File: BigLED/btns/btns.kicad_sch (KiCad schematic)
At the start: 25 parts, among them J1 MainBrd, J2 Prog, J3 DBG, SW1 TSX101G100-250, SW2 RotaryEncoder_Switch, SW3 SW_Push, SW4 SW_Push, SW5 SW_Push, SW6 SW_Push, SW7 SW_Push, SW8 SW_Push, SW9 SW_Push, U1 PY32F002AF15P6TU, U3 74LVC2G66, U4 SSD1306 OLED

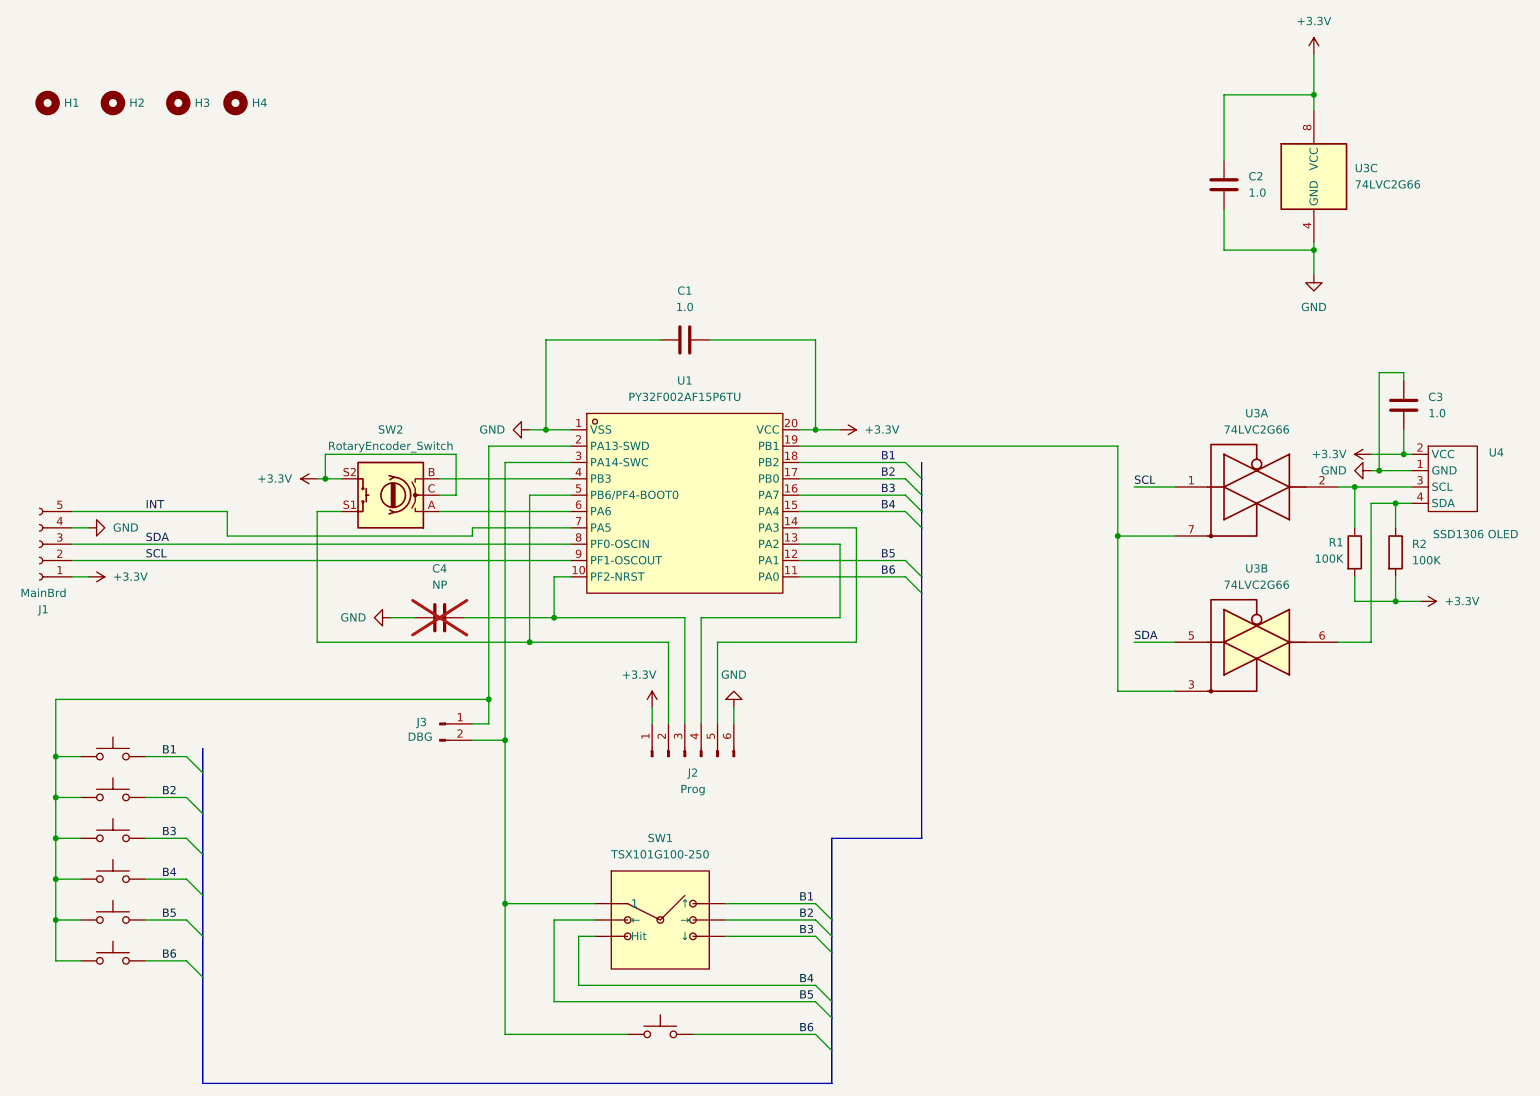
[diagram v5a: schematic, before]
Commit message: PCB for BigLED Buttons finished
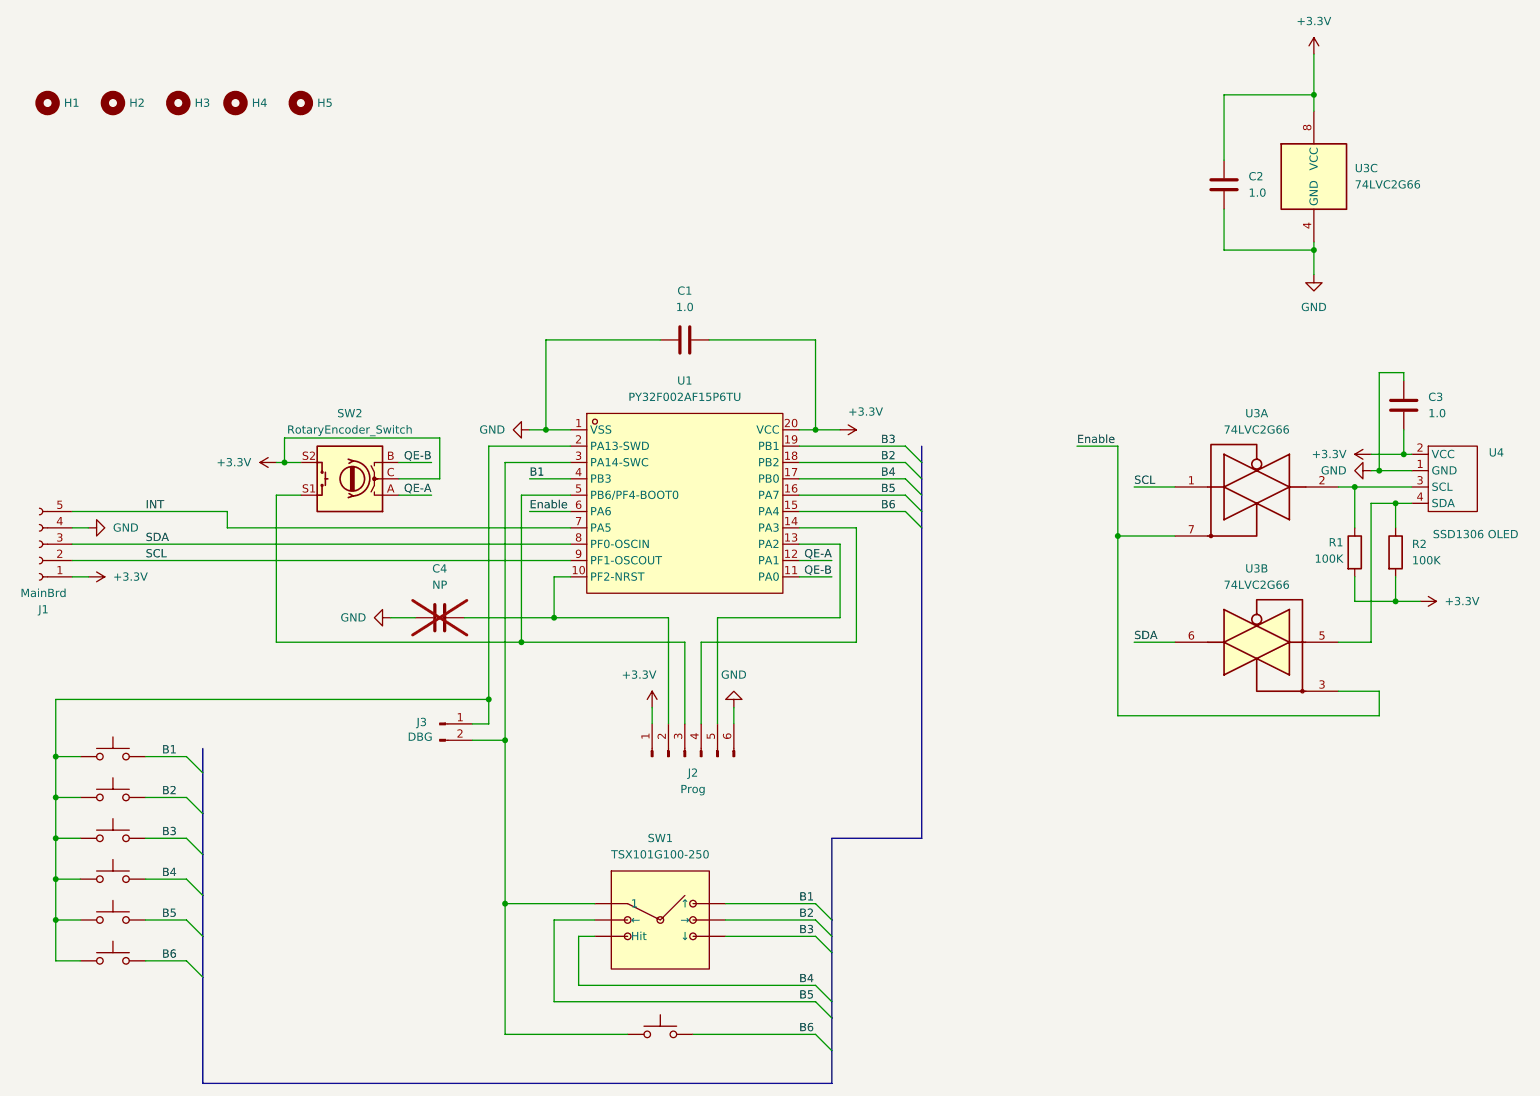
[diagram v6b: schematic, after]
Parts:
- added H5: MountingHole, MountingHole:MountingHole_3.2mm_M3, symbol Mechanical:MountingHole
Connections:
- net B1: now also U1.4 (PB3); no longer U1.18 (PB2)
- net B2: now also U1.18 (PB2); no longer U1.17 (PB0)
- net B3: now also U1.19 (PB1); no longer U1.16 (PA7)
- net B4: now also U1.17 (PB0); no longer U1.15 (PA4)
- net B5: now also U1.16 (PA7); no longer U1.12 (PA1)
- net B6: now also U1.15 (PA4); no longer U1.11 (PA0)
- net SDA: now also U3.6; no longer U3.5
- net Enable: now reaches U3.3, U3.7
- net Enable: now also U1.6 (PA6); no longer U1.19 (PB1)
- net at R2.1, U4.4 (SDA): now also U3.5; no longer U3.6
- net at C4.2, U1.10 (PF2-NRST): now also J2.2 (Pin_2); no longer J2.3 (Pin_3)
- net at SW2.S1, U1.5 (PB6/PF4-BOOT0): now also J2.3 (Pin_3); no longer J2.2 (Pin_2)
- net at J2.4 (Pin_4): now also U1.14 (PA3); no longer U1.13 (PA2)
- net at J2.5 (Pin_5): now also U1.13 (PA2); no longer U1.14 (PA3)
- net QE-A: now reaches SW2.A
- net QE-A: now also U1.12 (PA1); no longer U1.6 (PA6)
- net QE-B: now reaches SW2.B
- net QE-B: now also U1.11 (PA0); no longer U1.4 (PB3)
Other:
- moved on the sheet: SW2
